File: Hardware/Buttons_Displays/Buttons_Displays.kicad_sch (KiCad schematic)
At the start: 9 parts, among them J1 Conn_01x10, J2 Conn_01x10, J3 Conn_01x10, J4 Conn_01x10, J5 Conn_01x10, J6 Conn_01x10, J7 Conn_01x10, J8 Conn_01x10, U1 STM32H523RETx

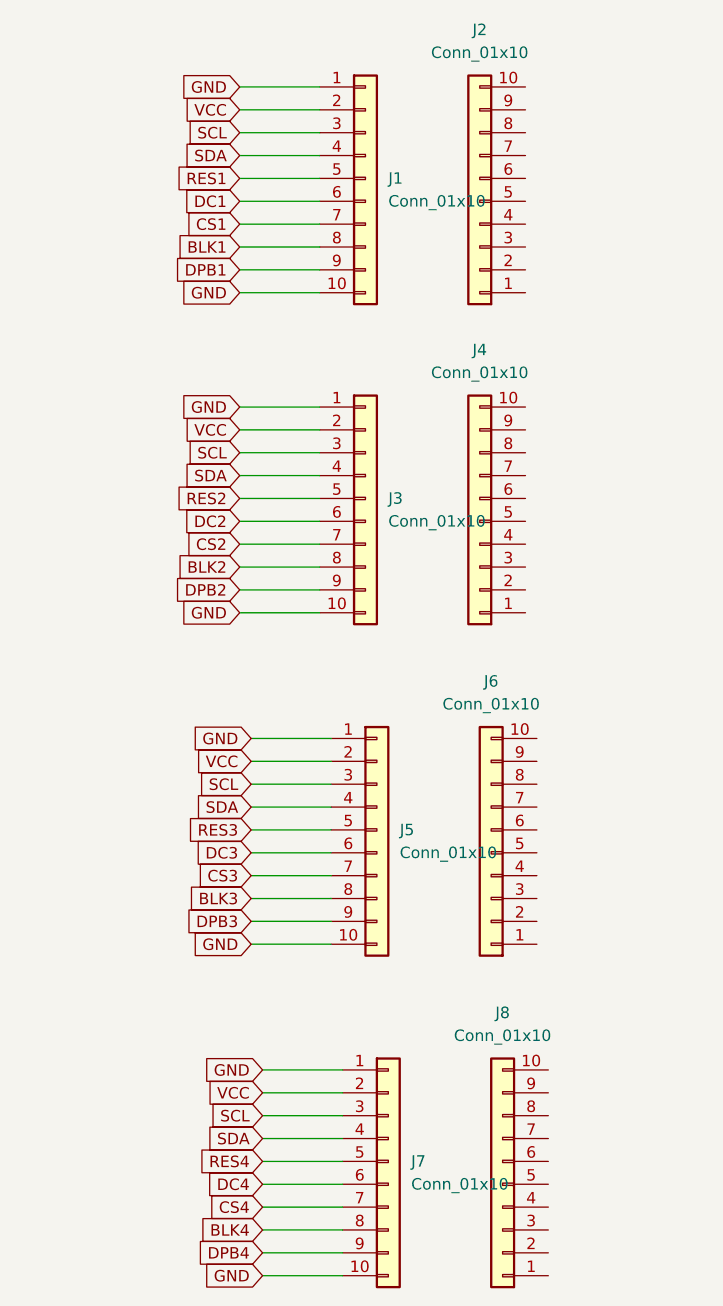
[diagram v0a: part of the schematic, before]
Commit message: Update Buttons_Displays.kicad_sch
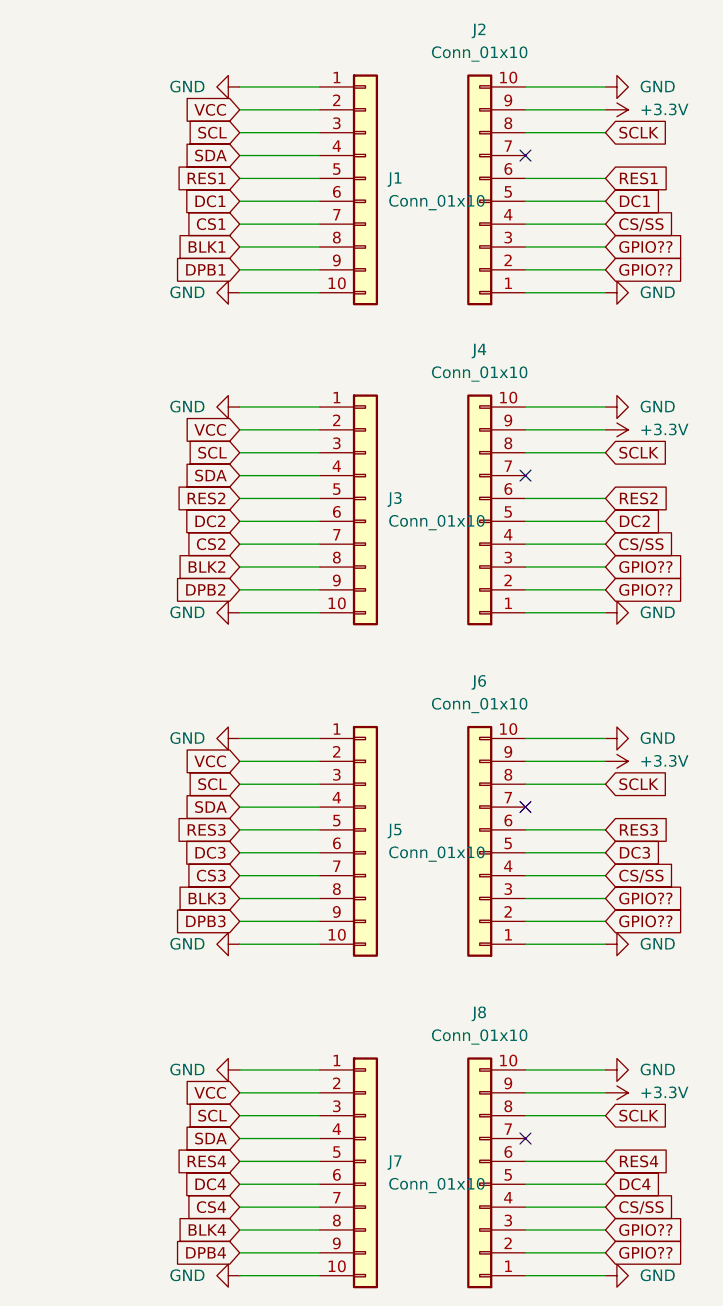
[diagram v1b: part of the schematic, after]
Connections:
- net DC1: now also J2.5 (Pin_5)
- net DC2: now also J4.5 (Pin_5)
- net DC3: now also J6.5 (Pin_5)
- net DC4: now also J8.5 (Pin_5)
- net GND: now also J2.1 (Pin_1), J2.10 (Pin_10), J4.1 (Pin_1), J4.10 (Pin_10), J6.1 (Pin_1), J6.10 (Pin_10), J8.1 (Pin_1), J8.10 (Pin_10)
- net RES1: now also J2.6 (Pin_6)
- net RES2: now also J4.6 (Pin_6)
- net RES3: now also J6.6 (Pin_6)
- net RES4: now also J8.6 (Pin_6)
- net GPIO??: now reaches J2.2 (Pin_2)
- net GPIO??: now also J2.3 (Pin_3), J4.2 (Pin_2), J4.3 (Pin_3), J6.2 (Pin_2), J6.3 (Pin_3), J8.2 (Pin_2), J8.3 (Pin_3)
- net CS/SS: now reaches J2.4 (Pin_4)
- net CS/SS: now also J4.4 (Pin_4), J6.4 (Pin_4), J8.4 (Pin_4)
- net SCLK: now reaches J2.8 (Pin_8)
- net SCLK: now also J4.8 (Pin_8), J6.8 (Pin_8), J8.8 (Pin_8)
- net +3.3V: now reaches J2.9 (Pin_9)
- net +3.3V: now also J4.9 (Pin_9), J6.9 (Pin_9), J8.9 (Pin_9)
- no-connect marks 0 -> 4
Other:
- moved on the sheet: J5, J6, J7, J8

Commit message: aantal pinnen
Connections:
- net CS/SS: now also U1.20 (PA4)
- net SCLK: now also U1.21 (PA5)
- net MOSI: now reaches U1.23 (PA7)
- net SWDIO: now reaches U1.46 (PA13(JTMS)
- net SWCLK: now reaches U1.49 (PA14(JTCK)
- net I2C1: now reaches U1.58 (PB6)
- net I2C1: now also U1.59 (PB7)
- net NRST: now reaches U1.7 (NRST)
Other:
- note added: "I2C BUS"
- note added: "Programming"
- note added: "SPI BUS"

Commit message: vergeten update
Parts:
- added J9: Conn_01x03, symbol Connector_Generic:Conn_01x03
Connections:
- net NRST: now also J9.3 (Pin_3)
- net SWCLK: now also J9.1 (Pin_1)
- net SWDIO: now also J9.2 (Pin_2)
- net GPIO1: now reaches U1.26 (PB0)
- net GPIO1: now also J2.3 (Pin_3)
- net GPIO2: now reaches U1.27 (PB1)
- net GPIO2: now also J2.2 (Pin_2)
- net GPIO3: now reaches U1.28 (PB2)
- net GPIO3: now also J4.3 (Pin_3)
- net GPIO6: now reaches U1.29 (PB10)
- net GPIO6: now also J6.2 (Pin_2)
- net GPIO7: now reaches U1.33 (PB12)
- net GPIO7: now also J8.3 (Pin_3)
- net GPIO8: now reaches U1.34 (PB13)
- net GPIO8: now also J8.2 (Pin_2)
- net GPIO4: now reaches U1.57 (PB5)
- net GPIO4: now also J4.2 (Pin_2)
- net GPIO5: now reaches U1.61 (PB8)
- net GPIO5: now also J6.3 (Pin_3)
- removed net GPIO??: J2.2 (Pin_2), J2.3 (Pin_3), J4.2 (Pin_2), J4.3 (Pin_3), J6.2 (Pin_2), J6.3 (Pin_3), J8.2 (Pin_2), J8.3 (Pin_3)
